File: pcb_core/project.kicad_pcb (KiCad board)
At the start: 2 copper layers, 212.3 x 91.7 mm, 143 parts, among them IC1 DRV8871DDA, IC10 DRV8871DDA, IC11 DRV8871DDA, IC12 DRV8871DDA, IC13 DRV8871DDA, IC14 DRV8871DDA, IC15 DRV8871DDA, IC16 DRV8871DDA, IC17 DRV8871DDA, IC18 DRV8871DDA, IC19 SX1509QBIULTRT, IC2 SX1509QBIULTRT, IC3 DRV8871DDA, IC4 TCA9548APWR, IC5 DRV8871DDA, IC6 DRV8871DDA, IC7 DRV8871DDA, IC8 DRV8871DDA, IC9 DRV8871DDA, J1 Conn_01x02, J10 1053131103, J11 1053131103, J12 1053131103, J13 1053131103, J14 1053131103, J15 1053131103, J16 1053131103, J17 1053131103, J18 1053131103, J19 Conn_02x02_Counter_Clockwise, J2 1725656, J20 PCBConnector, J21 PCBConnector, J22 PCBConnector, J23 PCBConnector, J25 PCBConnector, J27 PCBConnector, J3 1053131103, J4 1053131103, J5 1053131103, J6 1053131103, J7 1053131103, J8 1053131103, J9 1053131103, Q1 SI9945BDY-T1-GE3, U1 ESP32-S3-WROOM-2, U2 LTC4365TS8, U3 ESP32-DevKitC

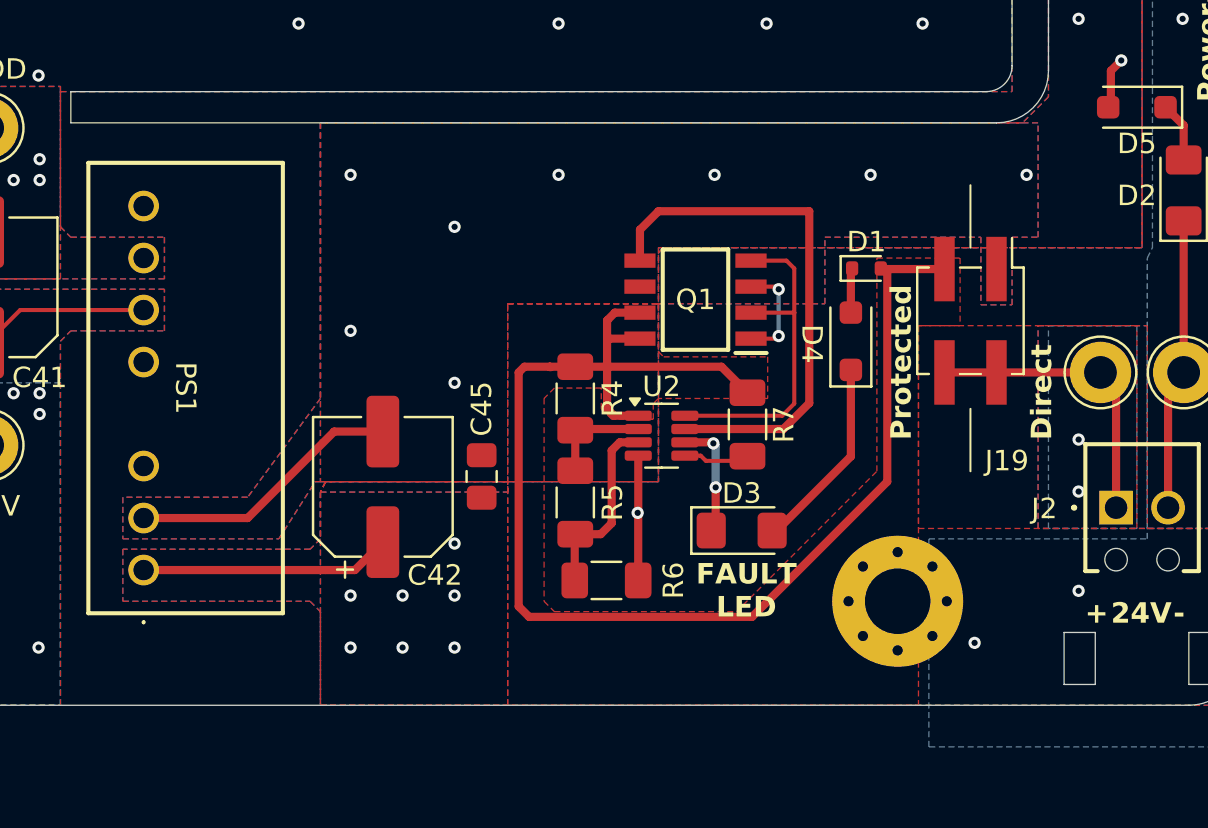
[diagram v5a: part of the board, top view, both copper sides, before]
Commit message: Update pcb, bom and add 3D view
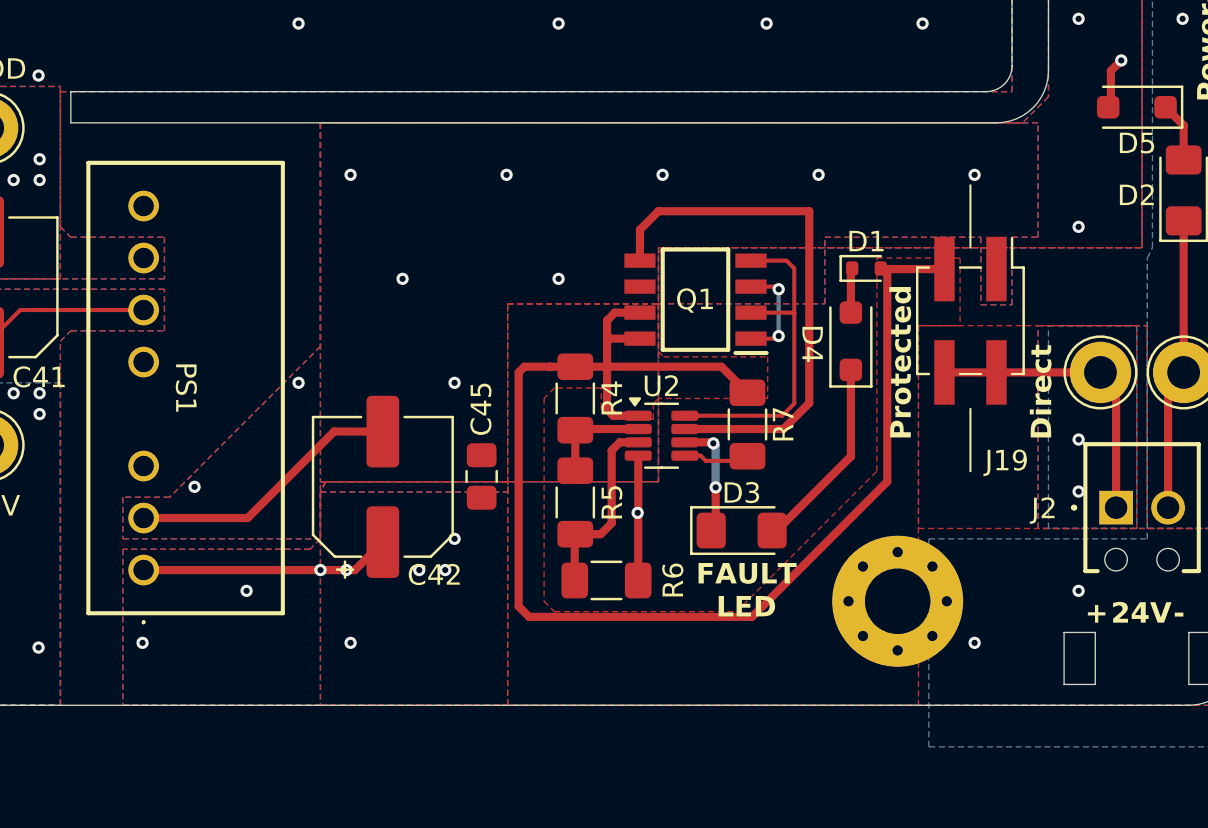
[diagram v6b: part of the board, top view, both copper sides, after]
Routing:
- net PROD_24V: vias 141 -> 144
- net GNDA: vias 359 -> 360

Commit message: Add blender render
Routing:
- net GNDA: vias 360 -> 362
